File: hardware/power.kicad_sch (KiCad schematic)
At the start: 42 parts, among them J5 B2B-EH-A, J6 Conn_01x02, J7 Conn_01x02, J8 Conn_01x02, J9 Conn_01x02, Q1 CSD25310Q2, U5 TPS63020DSJR, U6 BQ24074RGTR

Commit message: Start working on hw v4.0.0
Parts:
- removed C11, C12, C13: 22 µF, Capacitor_SMD:C_0805_2012Metric, symbol Device:C
- removed C14: 1 µF, Capacitor_SMD:C_0603_1608Metric, symbol Device:C
- removed C15, C17, C21, C22: 4.7 µF, Capacitor_SMD:C_0603_1608Metric, symbol Device:C
- removed C16, C18, C20, C23, C24: 100 nF, perfect_footprints:0402_1005_perfect, symbol Device:C
- removed C9: 100 µF, Capacitor_SMD:CP_Elec_5x5.3, symbol Device:C_Polarized
- removed FB1: 120 Ω @ 100 MHz, Resistor_SMD:R_0603_1608Metric, symbol Device:FerriteBead
- removed J5: B2B-EH-A, Connector_JST:JST_EH_B2B-EH-A_1x02_P2.50mm_Vertical, symbol Connector_Generic:Conn_02x01
- removed J8, J9: Conn_01x02, Connector_PinHeader_2.54mm:PinHeader_1x02_P2.54mm_Vertical, symbol Connector_Generic:Conn_01x02
- removed L1: 1.5 µH, Inductor_SMD:L_Taiyo-Yuden_NR-60xx, symbol Device:L
- removed LED6, LED7: LS T67K-K1L2-1-0-2-R18-Z, LED_SMD:LED_PLCC_2835, symbol Device:LED
- removed Q1: CSD25310Q2, Package_SON:Texas_DQK, symbol Transistor_FET:CSD25302Q2
- removed R17: 1 MΩ, perfect_footprints:0402_1005_perfect, symbol Device:R
- removed R18: 180 kΩ, perfect_footprints:0402_1005_perfect, symbol Device:R
- removed R19: 46.4 kΩ, perfect_footprints:0402_1005_perfect, symbol Device:R
- removed R20: 10 kΩ, perfect_footprints:0402_1005_perfect, symbol Device:R
- removed R21: 4.12 kΩ, perfect_footprints:0402_1005_perfect, symbol Device:R
- removed R22, R23: 1.13 kΩ, perfect_footprints:0402_1005_perfect, symbol Device:R
- removed R24: 2.2 kΩ, perfect_footprints:0402_1005_perfect, symbol Device:R
- removed TVS2: PE1605M1Q_R1_00001, Diode_SMD:D_0402_1005Metric, symbol Device:D_Zener
- removed U5: TPS63020DSJR, TPS63021DSJR:TPS63021DSJR, symbol TPS63021DSJR:TPS63021DSJR
- removed U6: BQ24074RGTR, Package_DFN_QFN:VQFN-16-1EP_3x3mm_P0.5mm_EP1.6x1.6mm, symbol BQ2407RGTR:BQ24074RGTR
- added BT1: Batteries, Battery:BatteryHolder_TruPower_BH-331P_3xAA, symbol Device:Battery_Cell
- added C8: 100 µF, Capacitor_SMD:CP_Elec_5x5.3, symbol Device:C_Polarized
- added C9: 100 nF, perfect_footprints:0402_1005_perfect, symbol Device:C
- added D1, D2: ~, symbol Device:D_Schottky
- added F1: 2A, symbol Device:Polyfuse
- added J2: USB4085-GF-A, USB4105-GF-A:USB4085-GF-A, symbol USB4085-GF-A:USB4085-GF-A
- added J4: Conn_01x02, Connector_PinHeader_2.54mm:PinHeader_1x02_P2.54mm_Vertical, symbol Connector_Generic:Conn_01x02
- added Q1, Q2: ~, symbol Simulation_SPICE:PMOS
- added R11: 10 kΩ, perfect_footprints:0402_1005_perfect, symbol Device:R
- added R13, R14: 5.1 kΩ, perfect_footprints:0402_1005_perfect, symbol Device:R
- added U4: USBLC6-2SC6, Package_TO_SOT_SMD:SOT-23-6, symbol Power_Protection:USBLC6-2SC6
- added U5: TLV76733DGNR, Package_SO:HVSSOP-8-1EP_3x3mm_P0.65mm_EP1.57x1.89mm_ThermalVias, symbol TLV76733DGNR:TLV76733DGNR
- C10: value 22 µF -> 4.7 µF; footprint Capacitor_SMD:C_0805_2012Metric -> Capacitor_SMD:C_0603_1608Metric; Digi-Key Part Number 1276-6526-1-ND -> 1276-1044-1-ND; Manufacturer Part Number CL21A226KOQNNNE -> CL10A475KP8NNNC
- C19: value 100 nF -> 4.7 µF; footprint perfect_footprints:0402_1005_perfect -> Capacitor_SMD:C_0603_1608Metric; Digi-Key Part Number 1276-1002-1-ND -> 1276-1044-1-ND; Manufacturer Part Number CL05B104KP5NNNC -> CL10A475KP8NNNC
- F2: value 5A -> 2A; footprint Fuse:Fuse_1812_4532Metric -> (none); Digi-Key Part Number 507-1781-1-ND -> (none); Manufacturer Bel Fuse Inc. -> (none); Manufacturer Part Number 0ZCG0300FF2B -> (none)
- R15: value 2.2 kΩ -> 10 kΩ; Digi-Key Part Number 311-2.20KLRCT-ND -> 311-10.0KLRCT-ND; Manufacturer Part Number RC0402FR-072K2L -> RC0402FR-0710KL
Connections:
- net +3.3V: now also J6.2 (Pin_2); no longer C19.1
- net GND: now also R15.2, R16.2, BT1.2 (-), C8.2, C9.1, J2.A1 (GND), J2.A12 (GND), J2.B1 (GND), J2.B12 (GND), J2.S1 (SHELL), J2.S2 (SHELL), J2.S3 (SHELL), J2.S4 (SHELL), J4.2 (Pin_2), R11.2, R13.1, R14.1, U4.2 (GND), U5.3 (NC), U5.4 (GND), U5.6 (GND), U5.9 (GND); no longer J6.2 (Pin_2), J7.2 (Pin_2)
- net at LED5.1 (K): now also R16.1
- net at LED5.2 (A): now also J7.2 (Pin_2); no longer R15.2
- net +BATT: no longer names the net of F2.1
- net +BATT: now also J2.A4 (VBUS), J2.A9 (VBUS), J2.B4 (VBUS), J2.B9 (VBUS)
- net BATT_PROT_S: no longer names the net of F2.2
- net BATT_PROT_S: now also R15.1, D1.2 (A), Q2.2 (G), U4.5 (VBUS)
- removed net BUCK_REG_IN: C10.1, R15.1, R16.1
- net VBUS: no longer names the net of J6.1 (Pin_1)
- net VBUS: now also C19.1, U5.1 (OUT), U5.2 (SNS); no longer TVS1.1 (K)
- new net: BT1.1 (+), F1.1
- new net: F1.2, Q1.1 (D)
- new net: C10.1, C9.2, D1.1 (K), D2.1 (K), J4.1 (Pin_1), TVS1.1 (K), U5.5 (EN), U5.8 (IN)
- new net: J2.A6 (DP1), J2.B6 (DP2), U4.3 (I/O2)
- new net: J2.A7 (DN1), J2.B7 (DN2), U4.1 (I/O1)
- new net: Q1.2 (G), R11.1
- new net: Q1.3 (S), Q2.1 (D)
- new net: C8.1, D2.2 (A), Q2.3 (S)
- new net CC1: J2.A5 (CC1), R14.2
- new net CC2: J2.B5 (CC2), R13.2
- new net USB_DN: U4.6 (I/O1)
- new net USB_DP: U4.4 (I/O2)
- no-connect marks 1 -> 2
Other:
- note added: "3xAA batteries 1.5 V * 3 = 4.5 V 1 AA battery =~ 2000 mAh Batteries are in series -> 4.5 V @ 2000 mAH"
- note added: "Can be powered with a USB-C connection. CC1 & CC2 tied to ground with 5.1 kΩ resistors -> 15 W can be drawn. P = U * I 15 W = 5 V * 3 A"
- note added: "If USB-C connection is ON, disconnect batteries."
- note added: "LDO with support for - Undervoltage lockout - Soft start - Overheat protection"
- note added: "Optional: External +5V supply"
- note added: "Place a jumper here to show that the 3.3 V power is ON."
- note added: "Place a jumper or an ammeter here"
- note added: "Reverse polarity protection"
- note removed: "100 nF capacitor per VDD pin. Place near MCU."
- note removed: "3.7V Li-ion battery power input"
- note removed: "Analog filtering and decoupling"
- note removed: "Battery"
- note removed: "Battery charger"
- note removed: "Battery polarity protection"
- note removed: "Buck-boost regulator"
- note removed: "Connect with a jumper or an ammeter"
- note removed: "Datasheet, section 10.2.2.2.1 Program the Fast Charge Current (ISET):"
- note removed: "Datasheet, section 10.2.2.2.2 Program the Input Current Limit (ILIM):"
- note removed: "Datasheet, section 10.2.2.2.3 Program the Termination Current Threshold (ITERM):"
- note removed: "Datasheet, section 10.2.2.2.4 Program 6.25-hour Fast-Charge Safety Timer (TMR):"
- note removed: "Datasheet, table 7-2 EN1/EN2 Settings:"
- note removed: "For voltage/power measurements"
- note removed: "IN: 2.5V - 5.5V OUT: 3.3V @ 2A"
- note removed: "Inputs"
- note removed: "Kicad power flags"
- note removed: "MCU decoupling"
- note removed: "NOTE: V_{OUT} comes from either V_{BUS} or +BATT so 3.4 V ≤ V_{OUT} ≤ 5V."
- note removed: "Place near MCU."
- note removed: "Power debug"
- note removed: "R_{ILIM} = K_{ILIM} / I_{I_{MAX}}, Where K_{ILIM} = 1550 AΩ and I_{I_{MAX}} = 1.3A."
- note removed: "R_{ISET} = K_{ISET} /I_{CHG}, Where K_{ISET} = 890 AΩ and I_{CHG} = 0.8A."
- note removed: "R_{ITERM} = I_{TERM} * R_{ISET} / 0.03, Where I_{TERM} = 110 mA."
- note removed: "R_{TMR} = t_{MAXCHG} / (10 * K_{TMR}), Where K_{TMR} = 48 s/kΩ and t_{MAXCHG} = 3600 s/hr."
- note removed: "USB receptacle or a lab power supply"
- note removed: "| EN2 | EN1 | Maximum input current into IN pin | |-----|-----|-------------------------------------------------| | 0 | 0 | 100 mA USB100 mode | | 0 | 1 | 500 mA USB500 mode | | 1 | 0 | Set by an external resistor from I_{LIM} to VSS | | 1 | 1 | Standby (USB suspend mode) |"

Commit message: HW: Continue developing
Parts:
- removed BT1: Batteries, Battery:BatteryHolder_TruPower_BH-331P_3xAA, symbol Device:Battery_Cell
- removed Q2: ~, symbol Simulation_SPICE:PMOS
- added BT2: Batteries, symbol Device:Battery
- added Q5: PMOS, Package_TO_SOT_SMD:SOT-23-3, symbol Simulation_SPICE:PMOS
- D1, D2: value ~ -> Schottky; footprint (none) -> Diode_SMD:D_SMA; Digi-Key Part Number (none) -> 641-1987-1-ND; Manufacturer (none) -> Comchip Technology; Manufacturer Part Number (none) -> CDBA140LL-HF
- F1, F2: footprint (none) -> Fuse:Fuse_0805_2012Metric; Digi-Key Part Number (none) -> 13-SMD0805B110TFCT-ND; Manufacturer (none) -> YAGEO; Manufacturer Part Number (none) -> SMD0805B110TF
- J4, J6, J7: Digi-Key Part Number PRPC001DAAN-RC -> S2011EC-01-ND; Manufacturer Part Number S2011EC-01-ND -> PRPC001DAAN-RC
- Q1: value ~ -> PMOS; footprint (none) -> Package_TO_SOT_SMD:SOT-23-3; Digi-Key Part Number (none) -> DMP2004KDICT-ND; Manufacturer (none) -> Diodes Incorporated; Manufacturer Part Number (none) -> DMP2004K-7
- U5: Digi-Key Part Number (none) -> 296-TLV76733DGNRCT-ND; DigiKey Part Number 296-TLV76733DGNRCT-ND -> (none)
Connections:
- net GND: now also BT2.2 (-)
- net at D1.2 (A), F2.2, R15.1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: now also Q1.2 (G)
- net at F1.1: now also BT2.1 (+)
- net at F1.2: now also Q5.1 (D); no longer Q1.1 (D)
- net at R11.1: now also Q5.2 (G); no longer Q1.2 (G)
- net at Q1.3 (S): now also Q5.3 (S)
- net at C8.1, D2.2 (A): now also Q1.1 (D)

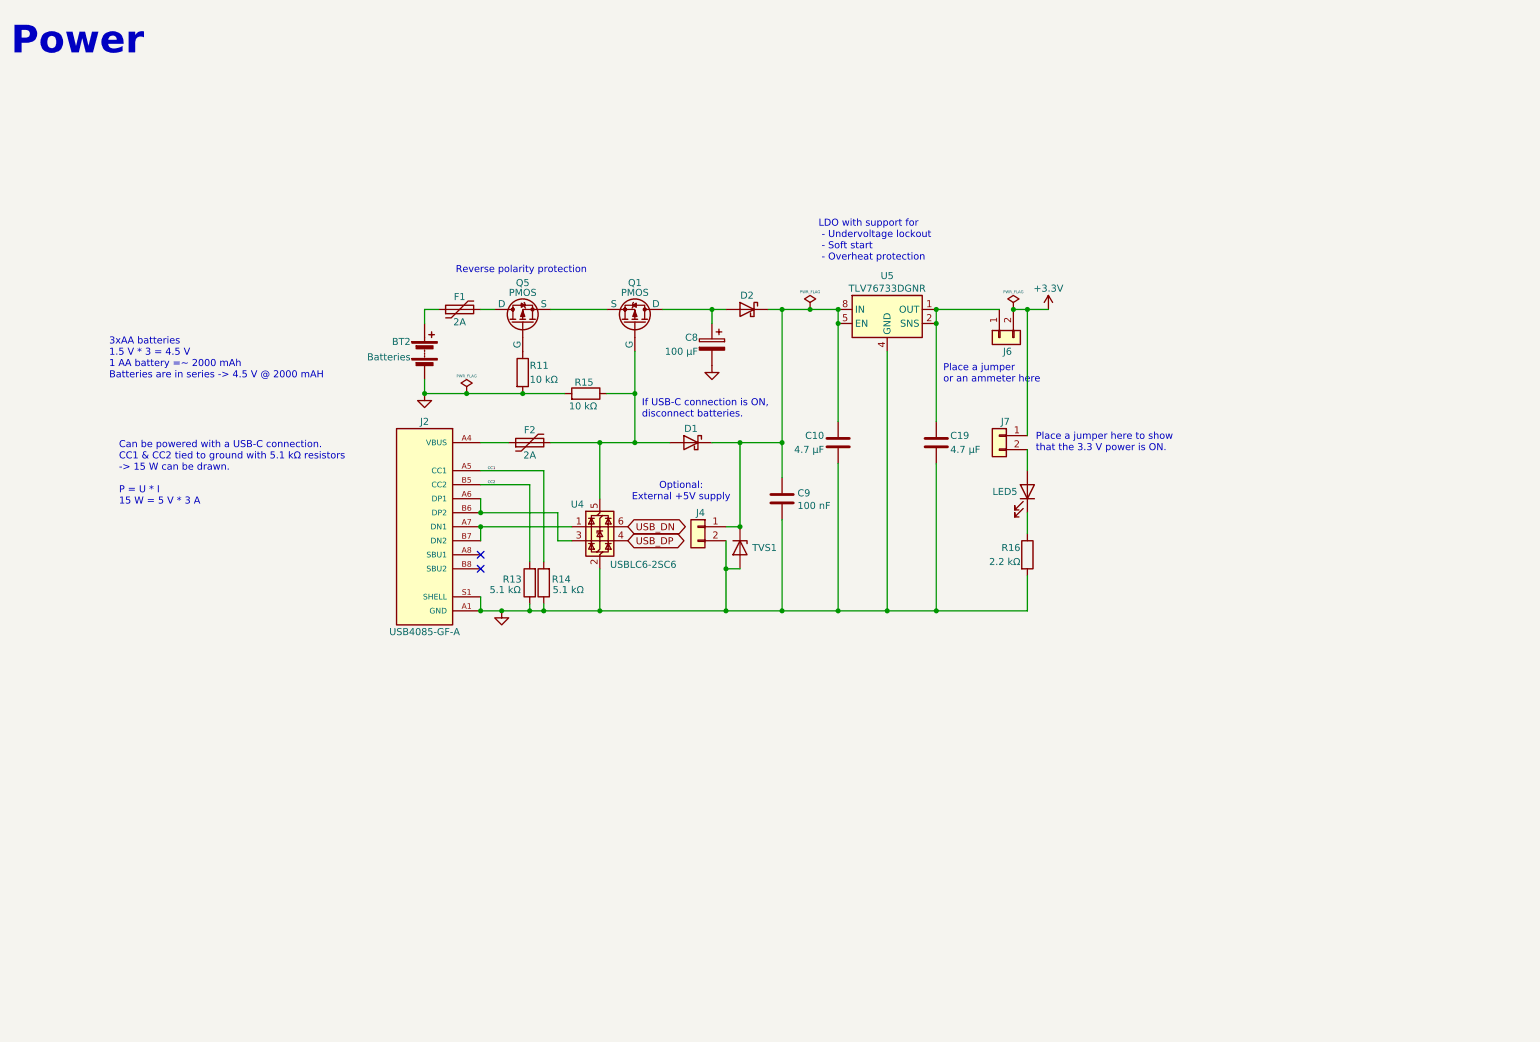
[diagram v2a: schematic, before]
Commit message: HW: Develop further
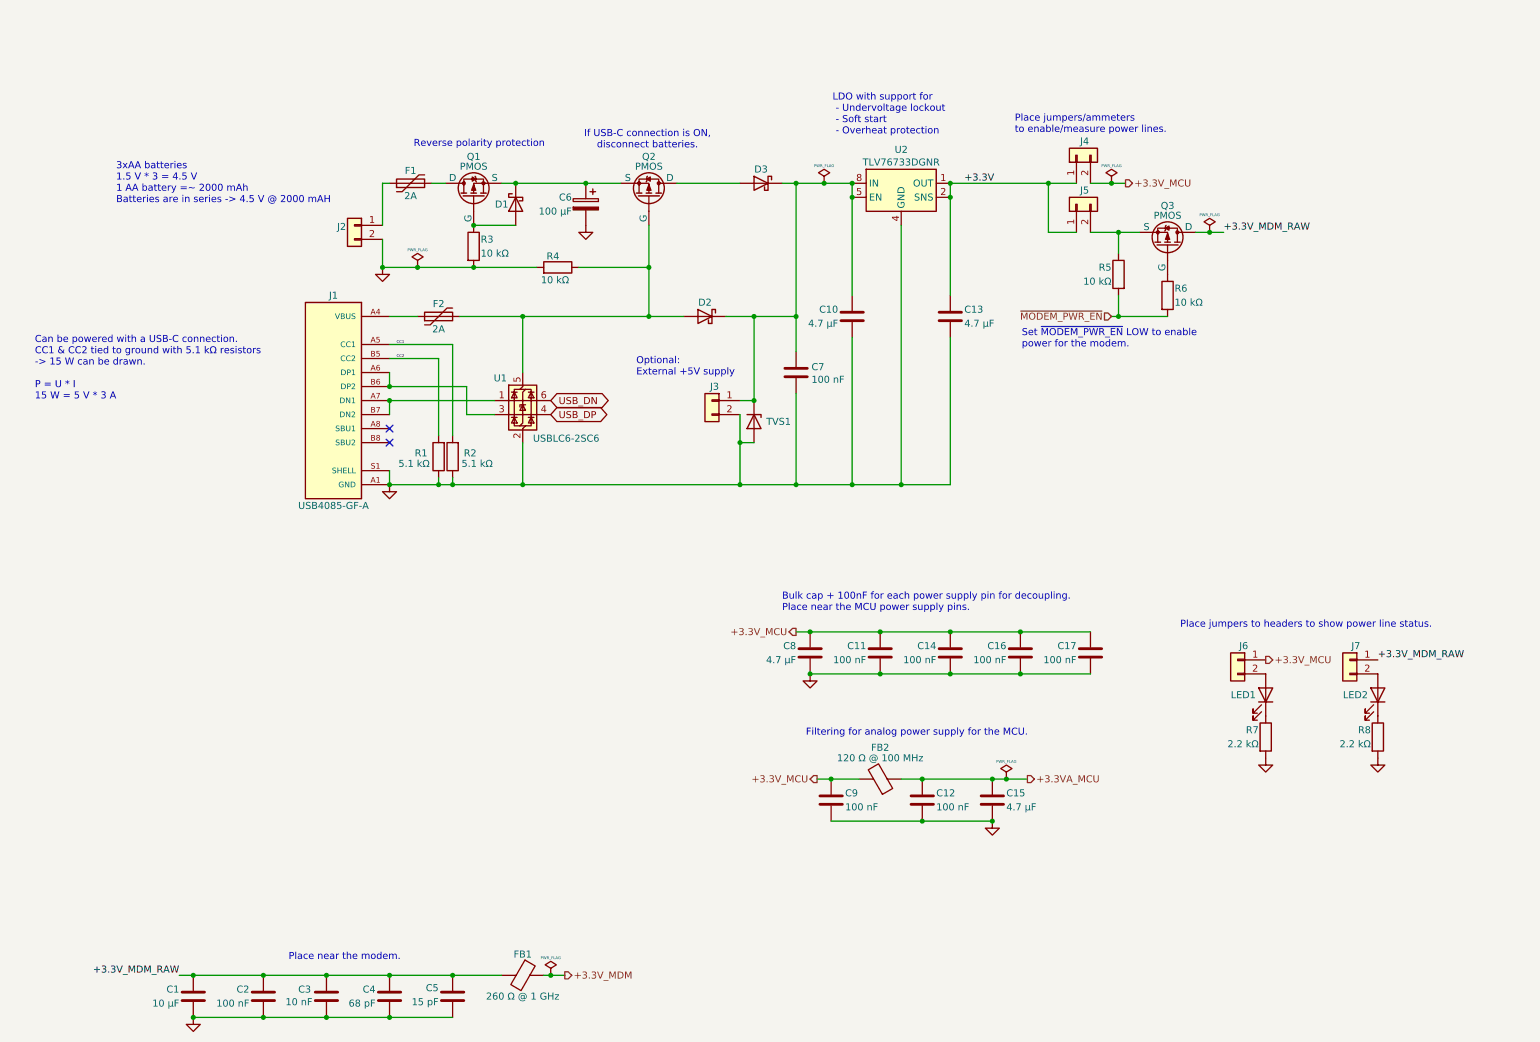
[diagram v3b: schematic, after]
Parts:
- removed BT2: Batteries, symbol Device:Battery
- added C1: 10 µF, Capacitor_SMD:C_0603_1608Metric, symbol Device:C
- added C11, C12, C14, C16, C17, C2, C9: 100 nF, perfect_footprints:0402_1005_perfect, symbol Device:C
- added C15, C8: 4.7 µF, Capacitor_SMD:C_0603_1608Metric, symbol Device:C
- added C3: 10 nF, perfect_footprints:0402_1005_perfect, symbol Device:C
- added C4: 68 pF, perfect_footprints:0402_1005_perfect, symbol Device:C
- added C5: 15 pF, perfect_footprints:0402_1005_perfect, symbol Device:C
- added D1: Schottky, Diode_SMD:D_SMA, symbol Device:D_Schottky
- added FB1: 260 Ω @ 1 GHz, Resistor_SMD:R_0603_1608Metric, symbol Device:FerriteBead
- added FB2: 120 Ω @ 100 MHz, Resistor_SMD:R_0603_1608Metric, symbol Device:FerriteBead
- added J2: Batteries, Connector_JST:JST_PH_B2B-PH-K_1x02_P2.00mm_Vertical, symbol Connector_Generic:Conn_01x02
- added J5, J7: Conn_01x02, Connector_PinHeader_2.54mm:PinHeader_1x02_P2.54mm_Vertical, symbol Connector_Generic:Conn_01x02
- added LED2: LS T67K-K1L2-1-0-2-R18-Z, LED_SMD:LED_PLCC_2835, symbol Device:LED
- added Q3: PMOS, Package_TO_SOT_SMD:SOT-23-3, symbol Simulation_SPICE:PMOS
- added R5, R6: 10 kΩ, perfect_footprints:0402_1005_perfect, symbol Device:R
- added R8: 2.2 kΩ, perfect_footprints:0402_1005_perfect, symbol Device:R
- C7: renamed from C9; Digi-Key Part Number 1276-1002-1-ND -> 490-7998-1-ND; Manufacturer Samsung Electro-Mechanics -> Murata Electronics; Manufacturer Part Number CL05B104KP5NNNC -> GCM155R71C104KA55J
- Q1: renamed from Q5; Digi-Key Part Number DMP2004KDICT-ND -> FDN338PCT-ND; Manufacturer Diodes Incorporated -> onsemi; Manufacturer Part Number DMP2004K-7 -> FDN338P
- Q2: renamed from Q1; Digi-Key Part Number DMP2004KDICT-ND -> FDN338PCT-ND; Manufacturer Diodes Incorporated -> onsemi; Manufacturer Part Number DMP2004K-7 -> FDN338P
- renumbered C19 to C13, C8 to C6, D1 to D2, D2 to D3, J2 to J1, J4 to J3, J6 to J4, J7 to J6, LED5 to LED1, R13 to R1, R14 to R2, R11 to R3, R15 to R4, R16 to R7, U4 to U1, U5 to U2
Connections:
- net +3.3V: now also C13.1, J4.1 (Pin_1), U2.1 (OUT), U2.2 (SNS), J5.1 (Pin_1); no longer J4.2 (Pin_2), J6.1 (Pin_1)
- net GND: now also C1.2, C11.2, C12.2, C14.2, C15.2, C16.2, C17.2, C2.2, C3.2, C4.2, C5.2, C8.2, C9.2, J2.2 (Pin_2), R8.2
- net at F1.1: now also J2.1 (Pin_1)
- net at Q1.2 (G), R3.1: now also D1.2 (A)
- net at D3.2 (A), Q2.1 (D): no longer C6.1
- net at Q1.3 (S), Q2.3 (S): now also C6.1, D1.1 (K)
- new net: LED2.1 (K), R8.1
- new net: J5.2 (Pin_2), Q3.3 (S), R5.1
- new net: Q3.2 (G), R6.1
- new net: J7.2 (Pin_2), LED2.2 (A)
- new net +3.3VA_MCU: C12.1, C15.1, FB2.1
- new net +3.3V_MCU: C11.1, C14.1, C16.1, C17.1, C8.1, C9.1, FB2.2, J4.2 (Pin_2), J6.1 (Pin_1)
- new net +3.3V_MDM: FB1.1
- new net +3.3V_MDM_RAW: C1.1, C2.1, C3.1, C4.1, C5.1, FB1.2, J7.1 (Pin_1), Q3.1 (D)
- new net ~{MODEM_PWR_EN}: R5.2, R6.2
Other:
- note added: "Bulk cap + 100nF for each power supply pin for decoupling. Place near the MCU power supply pins."
- note added: "Filtering for analog power supply for the MCU."
- note added: "Place jumpers to headers to show power line status."
- note added: "Place jumpers/ammeters to enable/measure power lines."
- note added: "Place near the modem."
- note added: "Set ~{MODEM_PWR_EN} LOW to enable power for the modem."
- note removed: "Place a jumper here to show that the 3.3 V power is ON."
- note removed: "Place a jumper or an ammeter here"
- note removed: "Power"
- moved on the sheet: C10, C13, C6, C7, D2, D3, F1, F2, J1, J3, J4, J6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

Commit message: HW: Develop further
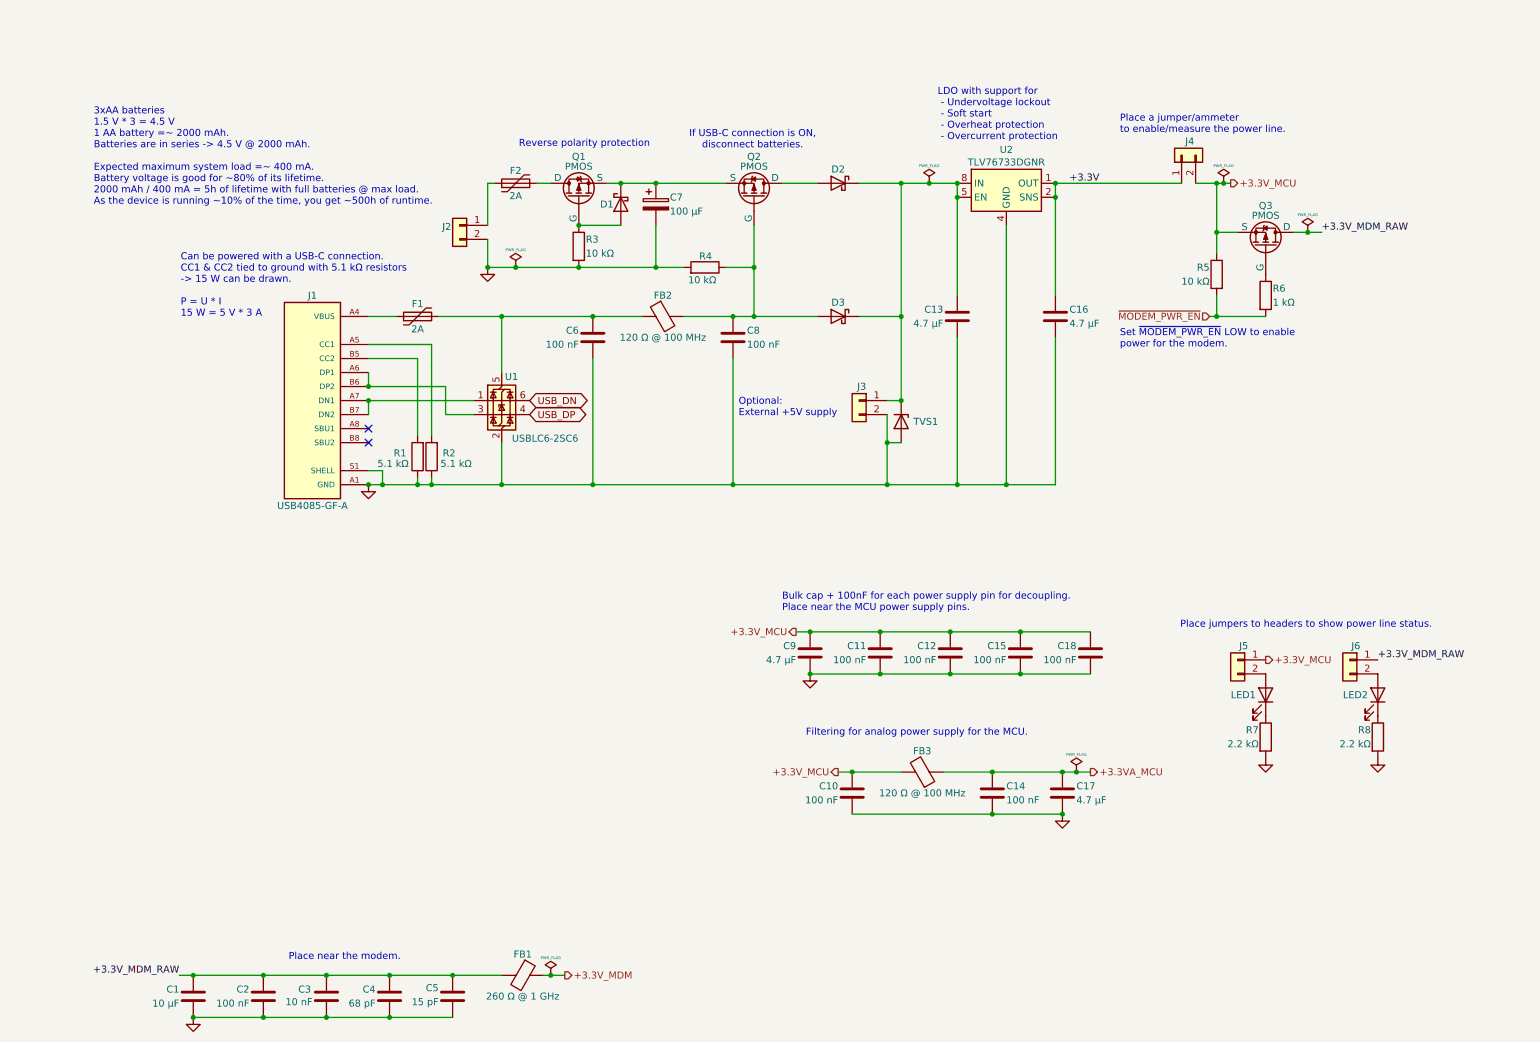
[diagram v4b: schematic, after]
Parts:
- removed C7: 100 nF, perfect_footprints:0402_1005_perfect, symbol Device:C
- removed J5: Conn_01x02, Connector_PinHeader_2.54mm:PinHeader_1x02_P2.54mm_Vertical, symbol Connector_Generic:Conn_01x02
- added C6, C8: 100 nF, perfect_footprints:0402_1005_perfect, symbol Device:C
- added FB2: 120 Ω @ 100 MHz, Resistor_SMD:R_0603_1608Metric, symbol Device:FerriteBead
- R6: value 10 kΩ -> 1 kΩ; Digi-Key Part Number 311-10.0KLRCT-ND -> 311-1.00KLRCT-ND; Manufacturer Part Number RC0402FR-0710KL -> RC0402FR-071KL
- U2: footprint Package_SO:HVSSOP-8-1EP_3x3mm_P0.65mm_EP1.57x1.89mm_ThermalVias -> Package_SO:MSOP-8-1EP_3x3mm_P0.65mm_EP1.95x2.15mm
- renumbered C9 to C10, C14 to C12, C10 to C13, C12 to C14, C16 to C15, C13 to C16, C15 to C17, C17 to C18, C6 to C7, C8 to C9, D3 to D2, D2 to D3, F2 to F1, F1 to F2, FB2 to FB3, J6 to J5, J7 to J6
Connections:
- net +3.3V_MCU: now also Q3.3 (S), R5.1
- net GND: now also C6.2, C8.2
- net at D3.2 (A), Q2.2 (G), R4.1: now also C8.1, FB2.2; no longer F1.2, U1.5 (VBUS)
- net CC1: no longer names the net of J1.A5 (CC1), R2.2
- net CC2: no longer names the net of J1.B5 (CC2), R1.2
- new net: C6.1, F1.2, FB2.1, U1.5 (VBUS)
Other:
- note added: "3xAA batteries 1.5 V * 3 = 4.5 V 1 AA battery =~ 2000 mAh. Batteries are in series -> 4.5 V @ 2000 mAh. Expected maximum system load =~ 400 mA. Battery voltage is good for ~80% of its lifetime. 2000 mAh / 400 mA = 5h of lifetime with full batteries @ max load. As the device is running ~10% of the time, you get ~500h of runtime."
- note added: "LDO with support for - Undervoltage lockout - Soft start - Overheat protection - Overcurrent protection"
- note added: "Place a jumper/ammeter to enable/measure the power line."
- note removed: "3xAA batteries 1.5 V * 3 = 4.5 V 1 AA battery =~ 2000 mAh Batteries are in series -> 4.5 V @ 2000 mAH"
- note removed: "LDO with support for - Undervoltage lockout - Soft start - Overheat protection"
- note removed: "Place jumpers/ammeters to enable/measure power lines."
- moved on the sheet: C10, C13, C14, C16, C17, C7, D1, D2, D3, F1, F2, FB3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
